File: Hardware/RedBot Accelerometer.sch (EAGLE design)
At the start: 17 parts, among them U1 MMA8452Q, U2 MIC5205-3.3V, U3 PCA9306

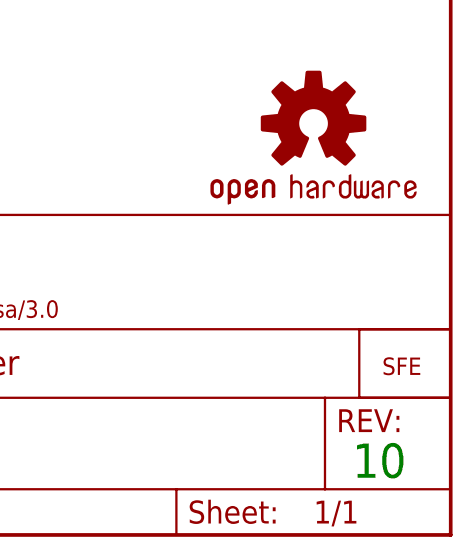
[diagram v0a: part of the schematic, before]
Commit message: Production readied
added fiducial references & created panel for manufacture
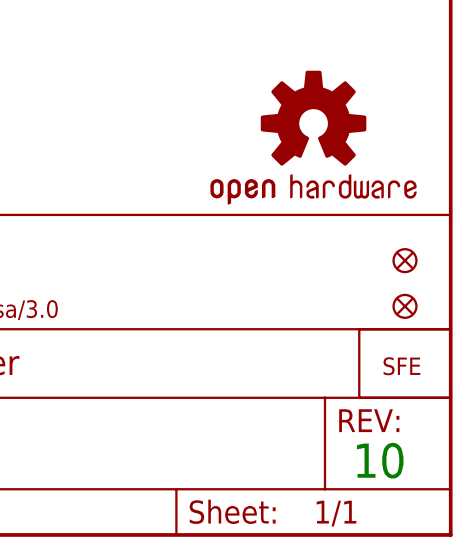
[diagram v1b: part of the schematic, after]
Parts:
- added FID1, FID2: FIDUCIALUFIDUCIAL, SparkFun-Aesthetics:FIDUCIALUFIDUCIAL
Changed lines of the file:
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@@
 <part name="SUPPLY7" library="SparkFun-Aesthetics" deviceset="5V" device=""/>
 <part name="GND5" library="SparkFun-Aesthetics" deviceset="GND" device=""/>
+<part name="FID1" library="SparkFun-Aesthetics" deviceset="FIDUCIAL" device="UFIDUCIAL"/>
+<part name="FID2" library="SparkFun-Aesthetics" deviceset="FIDUCIAL" device="UFIDUCIAL"/>
 </parts>
 <sheets>
@@
 <instance part="SUPPLY7" gate="G$1" x="187.96" y="157.48"/>
 <instance part="GND5" gate="1" x="187.96" y="132.08"/>
+<instance part="FID1" gate="G$1" x="243.84" y="30.48"/>
+<instance part="FID2" gate="G$1" x="243.84" y="25.4"/>
 </instances>
 <busses>
